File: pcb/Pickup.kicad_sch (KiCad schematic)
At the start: 45 parts, among them IC201 MAX9924UAUB+, Q201 MMBT2222A, T201 SM-LP-5001E, U201 AT223-CuH-S

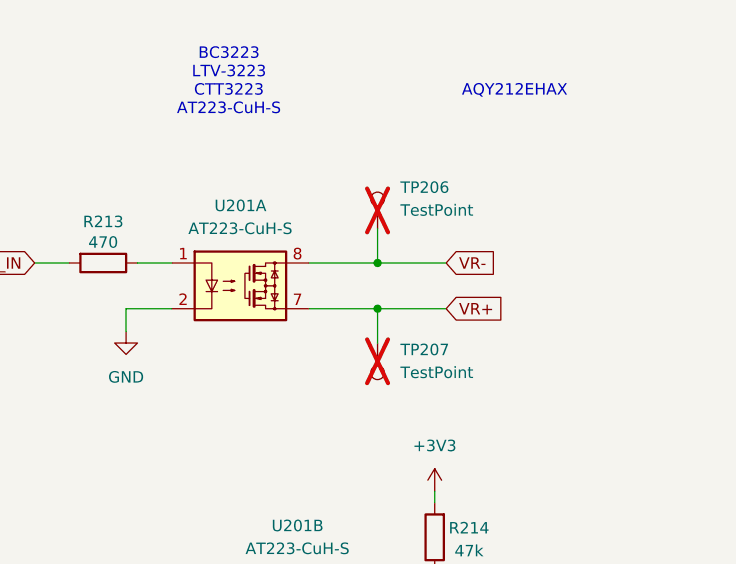
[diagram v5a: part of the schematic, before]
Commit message: removed duplicated test points
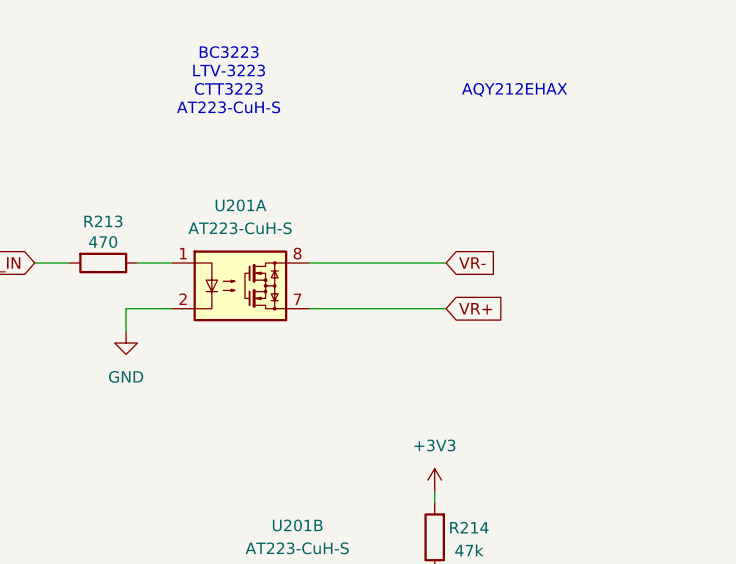
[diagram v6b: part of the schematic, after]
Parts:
- removed TP206, TP207: TestPoint, Connector_PinHeader_2.54mm:PinHeader_1x01_P2.54mm_Vertical, symbol Connector:TestPoint
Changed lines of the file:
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@@
 	)
 	(junction
-		(at 245.11 45.72)
-		(diameter 0)
-		(color 0 0 0 0)
-	)
-	(junction
 		(at 55.88 138.43)
 		(diameter 0)
@@
 	)
 	(junction
-		(at 245.11 50.8)
-		(diameter 0)
-		(color 0 0 0 0)
-	)
-	(junction
 		(at 34.29 152.4)
 		(diameter 0)
@@
 	(wire
 		(pts
-			(xy 245.11 50.8) (xy 237.49 50.8)
+			(xy 237.49 50.8) (xy 252.73 50.8)
 		)
 		(stroke
@@
 	(wire
 		(pts
-			(xy 252.73 50.8) (xy 245.11 50.8)
-		)
-		(stroke
-			(width 0)
-			(type default)
-		)
-	)
-	(wire
-		(pts
 			(xy 120.65 152.4) (xy 130.81 152.4)
 		)
@@
 	(wire
 		(pts
-			(xy 245.11 41.91) (xy 245.11 45.72)
-		)
-		(stroke
-			(width 0)
-			(type default)
-		)
-	)
-	(wire
-		(pts
 			(xy 54.61 25.4) (xy 58.42 25.4)
 		)
@@
 	(wire
 		(pts
-			(xy 252.73 45.72) (xy 245.11 45.72)
+			(xy 237.49 45.72) (xy 252.73 45.72)
 		)
 		(stroke
@@
 	(wire
 		(pts
-			(xy 245.11 54.61) (xy 245.11 50.8)
-		)
-		(stroke
-			(width 0)
-			(type default)
-		)
-	)
-	(wire
-		(pts
 			(xy 107.95 46.99) (xy 107.95 52.07)
 		)
@@
 	(wire
 		(pts
-			(xy 245.11 45.72) (xy 237.49 45.72)
-		)
-		(stroke
-			(width 0)
-			(type default)
-		)
-	)
-	(wire
-		(pts
 			(xy 219.71 91.44) (xy 219.71 90.17)
 		)
@@
 	)
 	(symbol
-		(lib_id "Connector:TestPoint")
-		(at 245.11 54.61 180)
-		(unit 1)
-		(exclude_from_sim no)
-		(in_bom yes)
-		(on_board yes)
-		(dnp yes)
-		(property "Reference" "TP207"
-			(at 247.65 55.372 0)
-			(effects
-				(font
-					(size 1.27 1.27)
-				)
-				(justify right)
-			)
-		)
-		(property "Value" "TestPoint"
-			(at 247.65 57.912 0)
-			(effects
-				(font
-					(size 1.27 1.27)
-				)
-				(justify right)
-			)
-		)
-		(property "Footprint" "Connector_PinHeader_2.54mm:PinHeader_1x01_P2.54mm_Vertical"
-			(at 240.03 54.61 0)
-			(effects
-				(font
-					(size 1.27 1.27)
-				)
-				(hide yes)
-			)
-		)
-		(property "Datasheet" "~"
-			(at 240.03 54.61 0)
-			(effects
-				(font
-					(size 1.27 1.27)
-				)
-				(hide yes)
-			)
-		)
-		(property "Description" "test point"
-			(at 245.11 54.61 0)
-			(effects
-				(font
-					(size 1.27 1.27)
-				)
-				(hide yes)
-			)
-		)
-		(pin "1"
-		)
-		(instances
-			(project "ecu-dev-board"
-				(path "/38d4df77-b5a0-4642-8410-8b13c21c2c3b/419a62de-f56b-49aa-b69b-37bd2fc230d8"
-					(reference "TP207")
-					(unit 1)
-				)
-			)
-		)
-	)
-	(symbol
 		(lib_id "Device:C")
 		(at 109.22 171.45 0)
@@
 					(unit 1)
 				)
-			)
-		)
-	)
-	(symbol
-		(lib_id "Connector:TestPoint")
-		(at 245.11 41.91 0)
-		(unit 1)
-		(exclude_from_sim no)
-		(in_bom yes)
-		(on_board yes)
-		(dnp yes)
-		(fields_autoplaced yes)
-		(property "Reference" "TP206"
-			(at 247.65 37.3379 0)
-			(effects
-				(font
-					(size 1.27 1.27)
-				)
-				(justify left)
-			)
-		)
-		(property "Value" "TestPoint"
-			(at 247.65 39.8779 0)
-			(effects
-				(font
-					(size 1.27 1.27)
-				)
-				(justify left)
-			)
-		)
-		(property "Footprint" "Connector_PinHeader_2.54mm:PinHeader_1x01_P2.54mm_Vertical"
-			(at 250.19 41.91 0)
-			(effects
-				(font
-					(size 1.27 1.27)
-				)
-				(hide yes)
-			)
-		)
-		(property "Datasheet" "~"
-			(at 250.19 41.91 0)
-			(effects
-				(font
-					(size 1.27 1.27)
-				)
-				(hide yes)
-			)
-		)
-		(property "Description" "test point"
-			(at 245.11 41.91 0)
-			(effects
-				(font
-					(size 1.27 1.27)
-				)
-				(hide yes)
-			)
-		)
-		(pin "1"
-		)
-		(instances
-			(project "ecu-dev-board"
-				(path "/38d4df77-b5a0-4642-8410-8b13c21c2c3b/419a62de-f56b-49aa-b69b-37bd2fc230d8"
-					(reference "TP206")
-					(unit 1)
-				)

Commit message: components updates
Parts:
- R207: footprint Resistor_SMD:R_0805_2012Metric -> Resistor_SMD:R_0603_1608Metric
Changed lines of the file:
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@@
 			)
 		)
-		(property "Footprint" "Resistor_SMD:R_0805_2012Metric"
+		(property "Footprint" "Resistor_SMD:R_0603_1608Metric"
 			(at 67.31 76.962 90)
 			(effects

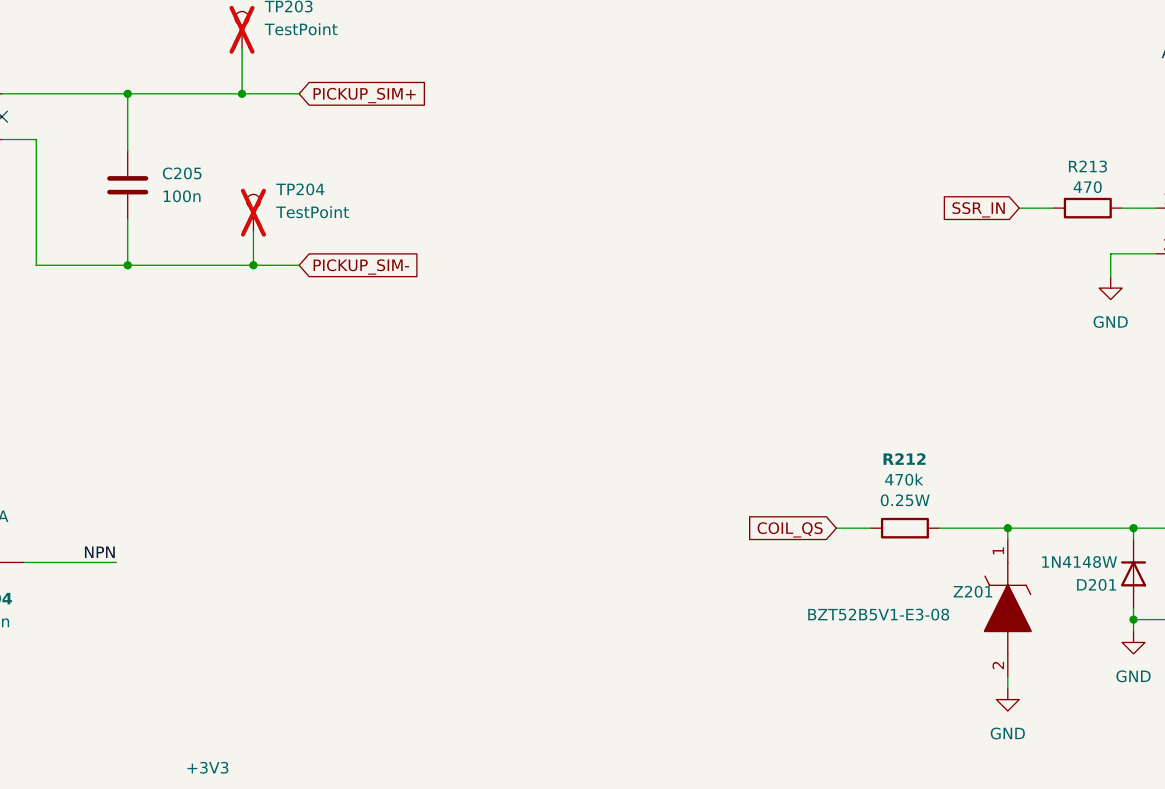
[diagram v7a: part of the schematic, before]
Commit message: removed unnecessary silkscreen designators
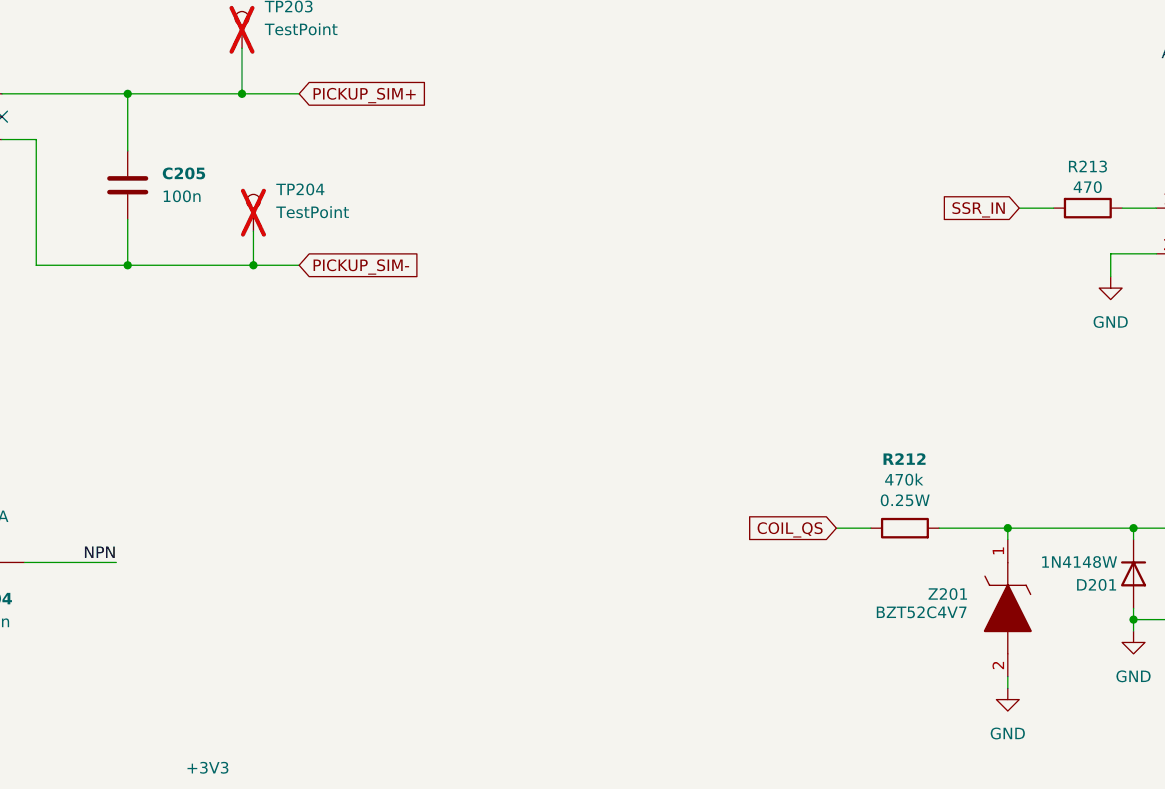
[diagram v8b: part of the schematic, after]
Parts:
- Z201: value BZT52B5V1-E3-08 -> BZT52C4V7
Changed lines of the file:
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@@
 		(fields_autoplaced yes)
 		(property "Reference" "C205"
-			(at 111.76 41.9099 0)
-			(effects
-				(font
-					(size 1.27 1.27)
+			(at 111.76 41.91 0)
+			(effects
+				(font
+					(size 1.27 1.27)
+					(thickness 0.254)
+					(bold yes)
 				)
 				(justify left)
@@
 		(dnp no)
 		(property "Reference" "Z201"
-			(at 199.644 88.392 90)
-			(effects
-				(font
-					(size 1.27 1.27)
-				)
-				(justify left)
-			)
-		)
-		(property "Value" "BZT52B5V1-E3-08"
-			(at 183.388 90.932 90)
-			(effects
-				(font
+			(at 196.85 88.646 90)
+			(effects
+				(font
+					(size 1.27 1.27)
+				)
+				(justify left)
+			)
+		)
+		(property "Value" "BZT52C4V7"
+			(at 191.008 90.678 90)
+			(effects
+				(font
